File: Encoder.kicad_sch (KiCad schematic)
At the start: 21 parts, among them J4 C225127, J7 C225127, U5 AS5047D, U8 AS5047D

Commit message: DRC check - fine tuning
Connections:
- no-connect marks 0 -> 14
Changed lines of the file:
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@@
 		(color 0 0 0 0)
+	)
+	(no_connect
+		(at 228.6 73.66)
+	)
+	(no_connect
+		(at 215.9 68.58)
+	)
+	(no_connect
+		(at 241.3 53.34)
+	)
+	(no_connect
+		(at 241.3 66.04)
+	)
+	(no_connect
+		(at 215.9 58.42)
+	)
+	(no_connect
+		(at 241.3 55.88)
+	)
+	(no_connect
+		(at 215.9 53.34)
+	)
+	(no_connect
+		(at 215.9 60.96)
+	)
+	(no_connect
+		(at 241.3 68.58)
+	)
+	(no_connect
+		(at 228.6 48.26)
+	)
+	(no_connect
+		(at 215.9 66.04)
+	)
+	(no_connect
+		(at 241.3 63.5)
+	)
+	(no_connect
+		(at 241.3 58.42)
+	)
+	(no_connect
+		(at 215.9 55.88)
 	)
 	(wire

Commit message: Drc, Bom done
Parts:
- J4, J7: LCSC (none) -> C225127
- U5, U8: LCSC (none) -> C55112284
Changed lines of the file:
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@@
+			)
+		)
+		(property "LCSC" "C55112284"
+			(at 143.1133 45.72 0)
+			(effects
+				(font
+					(size 1.27 1.27)
+				)
+				(hide yes)
 			)
 		)
@@
 			)
 		)
+		(property "LCSC" "C225127"
+			(at 43.18 180.34 0)
+			(effects
+				(font
+					(size 1.27 1.27)
+				)
+				(hide yes)
+			)
+		)
 		(pin "1"
 		)
@@
 			)
 		)
+		(property "LCSC" "C55112284"
+			(at 230.7433 45.72 0)
+			(effects
+				(font
+					(size 1.27 1.27)
+				)
+				(hide yes)
+			)
+		)
 		(pin "2"
 		)
@@
 			)
 		)
+		(property "LCSC" "C225127"
+			(at 43.18 120.65 0)
+			(effects
+				(font
+					(size 1.27 1.27)
+				)
+				(hide yes)
+			)
+		)

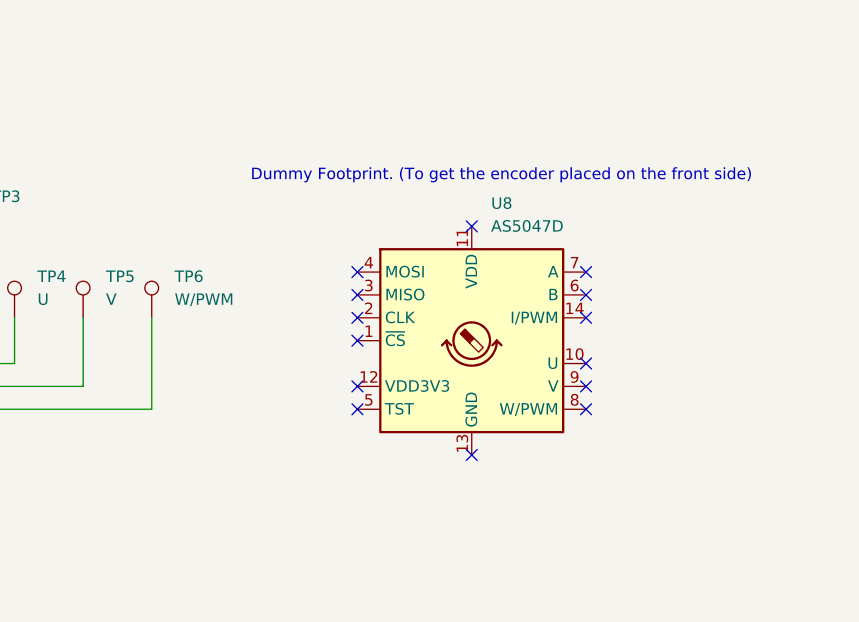
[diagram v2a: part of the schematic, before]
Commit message: Updated led placement
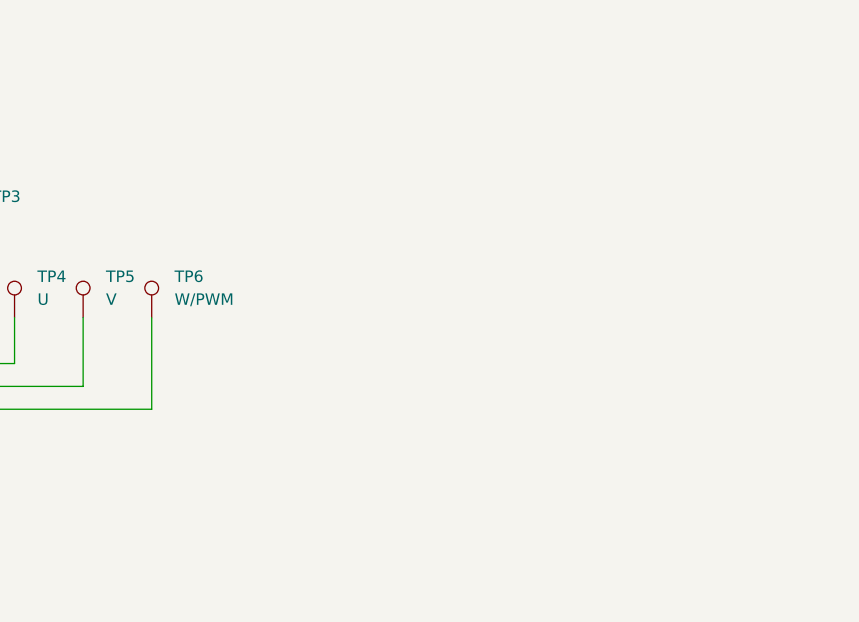
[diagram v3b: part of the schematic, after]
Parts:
- removed U8: AS5047D, Package_SO:TSSOP-14_4.4x5mm_P0.65mm, symbol Sensor_Magnetic:AS5047D
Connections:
- no-connect marks 14 -> 0
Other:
- note removed: "Dummy Footprint. (To get the encoder placed on the front side)"
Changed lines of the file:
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@@
 	(generator_version "10.0")
 	(paper "A4")
-	(text "Dummy Footprint. (To get the encoder placed on the front side)"
-		(exclude_from_sim no)
-		(at 231.902 42.672 0)
-		(effects
-			(font
-				(size 1.27 1.27)
-			)
-		)
-	)
 	(junction
 		(at 76.2 166.37)
@@
 		(color 0 0 0 0)
 	)
-	(no_connect
-		(at 228.6 73.66)
-	)
-	(no_connect
-		(at 215.9 68.58)
-	)
-	(no_connect
-		(at 241.3 53.34)
-	)
-	(no_connect
-		(at 241.3 66.04)
-	)
-	(no_connect
-		(at 215.9 58.42)
-	)
-	(no_connect
-		(at 241.3 55.88)
-	)
-	(no_connect
-		(at 215.9 53.34)
-	)
-	(no_connect
-		(at 215.9 60.96)
-	)
-	(no_connect
-		(at 241.3 68.58)
-	)
-	(no_connect
-		(at 228.6 48.26)
-	)
-	(no_connect
-		(at 215.9 66.04)
-	)
-	(no_connect
-		(at 241.3 63.5)
-	)
-	(no_connect
-		(at 241.3 58.42)
-	)
-	(no_connect
-		(at 215.9 55.88)
-	)
 	(wire
 		(pts
@@
 		(property "LCSC" "C55112284"
 			(at 143.1133 45.72 0)
+			(hide yes)
+			(show_name no)
+			(do_not_autoplace no)
 			(effects
 				(font
 					(size 1.27 1.27)
 				)
-				(hide yes)
 			)
 		)
@@
 		(property "LCSC" "C225127"
 			(at 43.18 180.34 0)
+			(hide yes)
+			(show_name no)
+			(do_not_autoplace no)
 			(effects
 				(font
 					(size 1.27 1.27)
 				)
-				(hide yes)
 			)
 		)
@@
 	)
 	(symbol
-		(lib_id "Sensor_Magnetic:AS5047D")
-		(at 228.6 60.96 0)
-		(unit 1)
-		(body_style 1)
-		(exclude_from_sim no)
-		(in_bom yes)
-		(on_board yes)
-		(in_pos_files yes)
-		(dnp no)
-		(fields_autoplaced yes)
-		(property "Reference" "U8"
-			(at 230.7433 45.72 0)
-			(show_name no)
-			(do_not_autoplace no)
-			(effects
-				(font
-					(size 1.27 1.27)
-				)
-				(justify left)
-			)
-		)
-		(property "Value" "AS5047D"
-			(at 230.7433 48.26 0)
-			(show_name no)
-			(do_not_autoplace no)
-			(effects
-				(font
-					(size 1.27 1.27)
-				)
-				(justify left)
-			)
-		)
-		(property "Footprint" "Package_SO:TSSOP-14_4.4x5mm_P0.65mm"
-			(at 228.6 76.2 0)
-			(hide yes)
-			(show_name no)
-			(do_not_autoplace no)
-			(effects
-				(font
-					(size 1.27 1.27)
-				)
-			)
-		)
-		(property "Datasheet" "https://ams.com/documents/20143/36005/AS5047D_DS000394_2-00.pdf"
-			(at 209.55 74.93 0)
-			(hide yes)
-			(show_name no)
-			(do_not_autoplace no)
-			(effects
-				(font
-					(size 1.27 1.27)
-				)
-			)
-		)
-		(property "Description" "On-Axis Magnetic Position Sensor, 14-bit, PWM Output, ABI Output, UVW Output, SPI Interface, TSSOP-14"
-			(at 228.6 60.96 0)
-			(hide yes)
-			(show_name no)
-			(do_not_autoplace no)
-			(effects
-				(font
-					(size 1.27 1.27)
-				)
-			)
-		)
-		(property "LCSC" "C55112284"
-			(at 230.7433 45.72 0)
-			(effects
-				(font
-					(size 1.27 1.27)
-				)
-				(hide yes)
-			)
-		)
-		(pin "2"
-		)
-		(pin "13"
-		)
-		(pin "6"
-		)
-		(pin "1"
-		)
-		(pin "12"
-		)
-		(pin "8"
-		)
-		(pin "14"
-		)
-		(pin "7"
-		)
-		(pin "10"
-		)
-		(pin "9"
-		)
-		(pin "5"
-		)
-		(pin "4"
-		)
-		(pin "3"
-		)
-		(pin "11"
-		)
-		(instances
-			(project "PiccoloMotorDriver"
-				(path "/cc8a13e7-b1a6-4cbd-adcd-4feb8b2e2369/b5037c4c-8129-4a92-a0a6-b41a7050a316"
-					(reference "U8")
-					(unit 1)
-				)
-			)
-		)
-	)
-	(symbol
 		(lib_id "power:GND")
 		(at 135.89 41.91 0)
@@
 		(property "LCSC" "C225127"
 			(at 43.18 120.65 0)
+			(hide yes)
+			(show_name no)
+			(do_not_autoplace no)
 			(effects
 				(font
 					(size 1.27 1.27)
 				)
-				(hide yes)
 			)
 		)
